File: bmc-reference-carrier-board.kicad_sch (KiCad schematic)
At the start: 0 parts

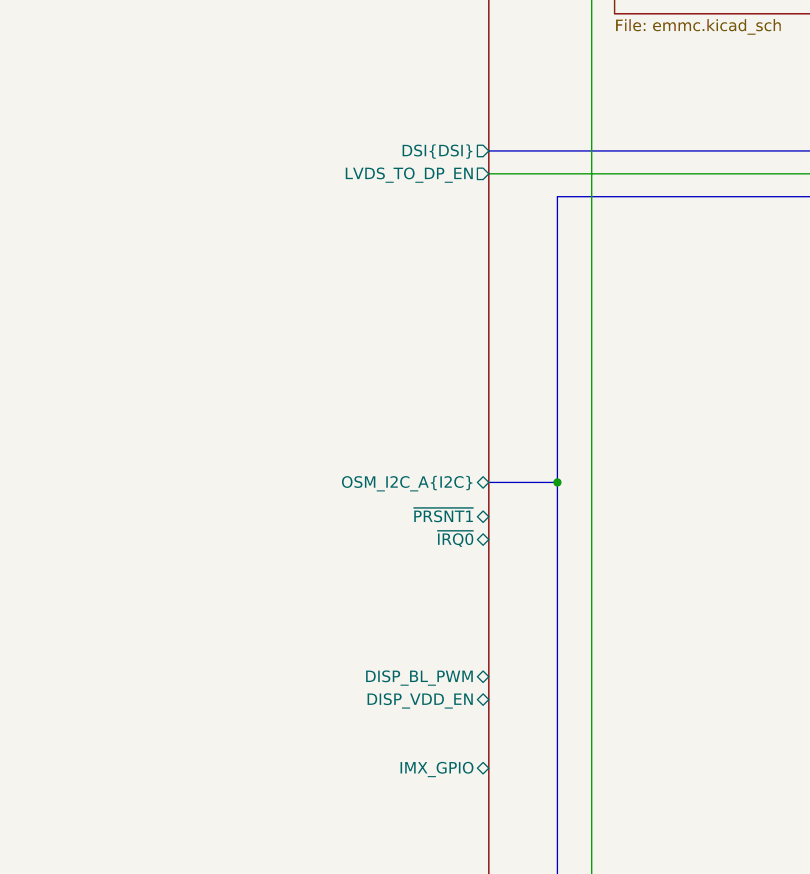
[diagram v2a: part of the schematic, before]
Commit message: [#82323] Small OSM pinout fixes
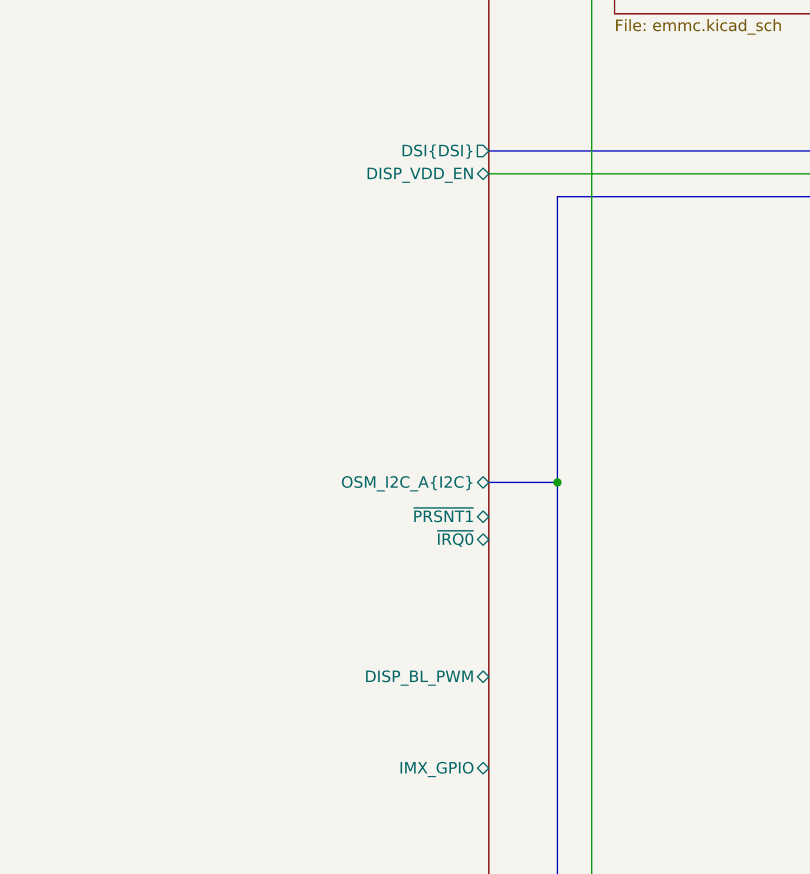
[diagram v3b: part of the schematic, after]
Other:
- sheet OSM L ports: added none; removed LVDS_TO_DP_EN
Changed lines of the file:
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@@
-			)
-		)
-		(pin "LVDS_TO_DP_EN" output
-			(at 251.46 189.23 0)
-			(effects
-				(font
-					(size 1.27 1.27)
-				)
-				(justify right)
 			)
 		)
@@
 		)
 		(pin "DISP_VDD_EN" bidirectional
-			(at 251.46 247.65 0)
+			(at 251.46 189.23 0)
 			(effects
 				(font

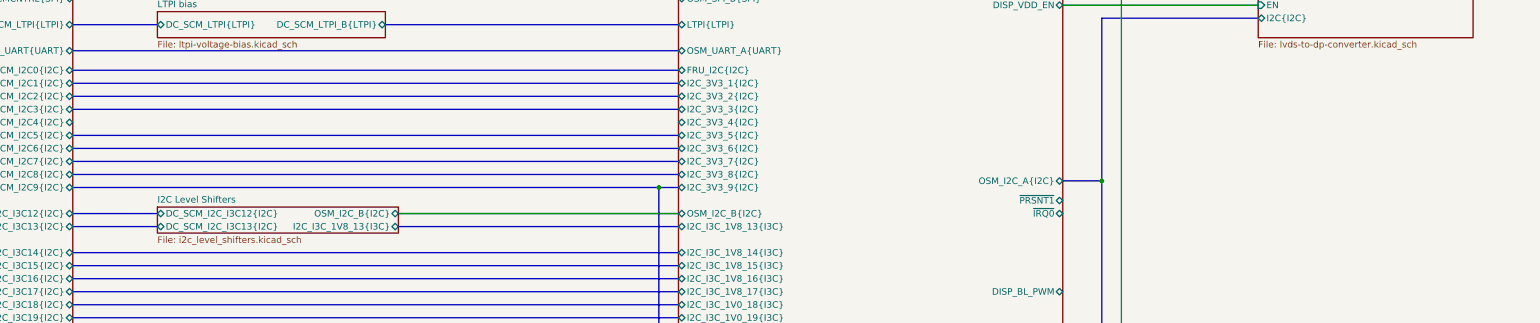
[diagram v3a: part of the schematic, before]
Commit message: [#83362] Add temperature sensors
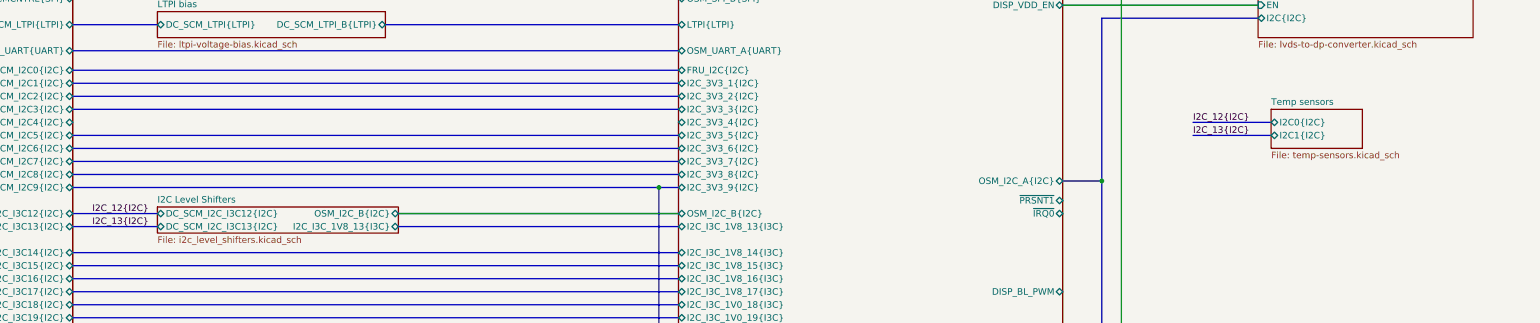
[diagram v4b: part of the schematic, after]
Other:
- added sheet Temp sensors (temp-sensors.kicad_sch)
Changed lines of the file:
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@@
+	(bus
+		(pts
+			(xy 276.86 212.09) (xy 292.1 212.09)
+		)
+		(stroke
+			(width 0)
+			(type default)
+		)
+	)
 	(bus
 		(pts
@@
 		)
 	)
+	(bus
+		(pts
+			(xy 276.86 214.63) (xy 292.1 214.63)
+		)
+		(stroke
+			(width 0)
+			(type default)
+		)
+	)
 	(wire
 		(pts
@@
 			(width 0)
 			(type default)
+		)
+	)
+	(label "I2C_12{I2C}"
+		(at 276.86 212.09 0)
+		(effects
+			(font
+				(size 1.27 1.27)
+			)
+			(justify left bottom)
+		)
+	)
+	(label "I2C_13{I2C}"
+		(at 62.23 232.41 0)
+		(effects
+			(font
+				(size 1.27 1.27)
+			)
+			(justify left bottom)
+		)
+	)
+	(label "I2C_12{I2C}"
+		(at 62.23 229.87 0)
+		(effects
+			(font
+				(size 1.27 1.27)
+			)
+			(justify left bottom)
+		)
+	)
+	(label "I2C_13{I2C}"
+		(at 276.86 214.63 0)
+		(effects
+			(font
+				(size 1.27 1.27)
+			)
+			(justify left bottom)
 		)
 	)
@@
 				)
 			)
+		)
+	)
+	(sheet
+		(at 292.1 209.55)
+		(size 17.78 7.62)
+		(exclude_from_sim no)
+		(in_bom yes)
+		(on_board yes)
+		(dnp no)
+		(fields_autoplaced yes)
+		(stroke
+			(width 0.1524)
+			(type solid)
+		)
+		(fill
+			(color 0 0 0 0.0000)
+		)
+		(property "Sheetname" "Temp sensors"
+			(at 292.1 208.8384 0)
+			(effects
+				(font
+					(size 1.27 1.27)
+				)
+				(justify left bottom)
+			)
+		)
+		(property "Sheetfile" "temp-sensors.kicad_sch"
+			(at 292.1 217.7546 0)
+			(effects
+				(font
+					(size 1.27 1.27)
+				)
+				(justify left top)
+			)
+		)
+		(pin "I2C0{I2C}" bidirectional
+			(at 292.1 212.09 180)
+			(effects
+				(font
+					(size 1.27 1.27)
+				)
+				(justify left)
+			)
+		)
+		(pin "I2C1{I2C}" bidirectional
+			(at 292.1 214.63 180)
+			(effects
+				(font
+					(size 1.27 1.27)
+				)
+				(justify left)
+			)
+		)
+		(instances
+			(project "bmc-reference-carrier-board"
+				(path "/5f636c45-3c15-4731-8931-4625e0dab7e4"
+					(page "23")
+				)
+			)

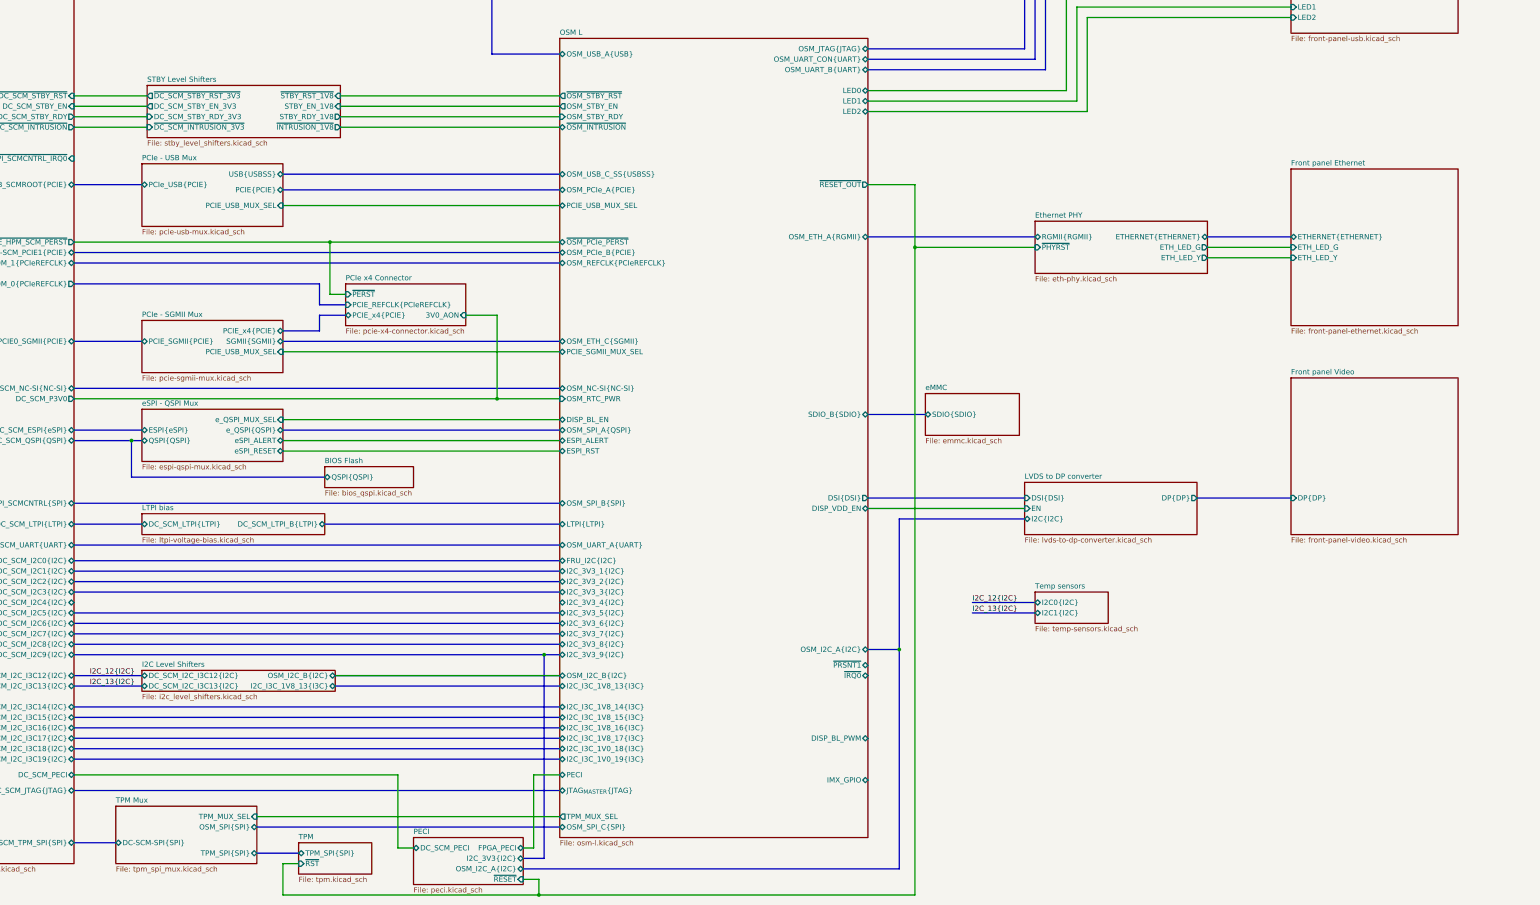
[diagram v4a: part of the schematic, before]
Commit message: [#83362] Fix connections of headers, add I2C mux
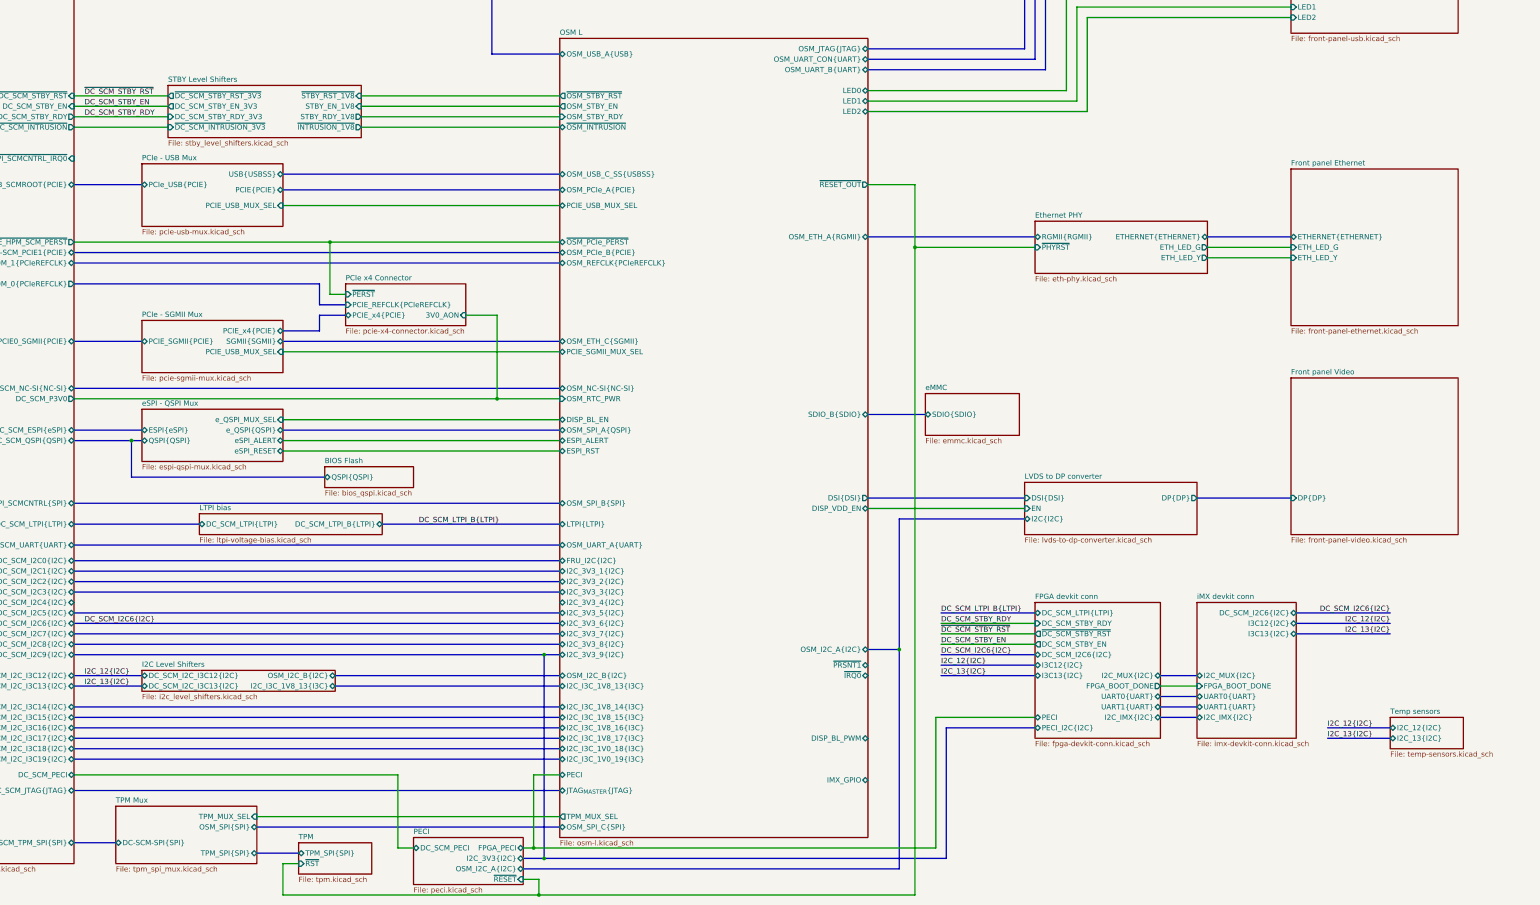
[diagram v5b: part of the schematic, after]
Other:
- added sheet FPGA devkit conn (fpga-devkit-conn.kicad_sch)
- added sheet iMX devkit conn (imx-devkit-conn.kicad_sch)
- sheet Temp sensors ports: added I2C_12{I2C}, I2C_13{I2C}; removed I2C0{I2C}, I2C1{I2C}
